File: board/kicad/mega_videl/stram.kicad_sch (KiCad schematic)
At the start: 3 parts

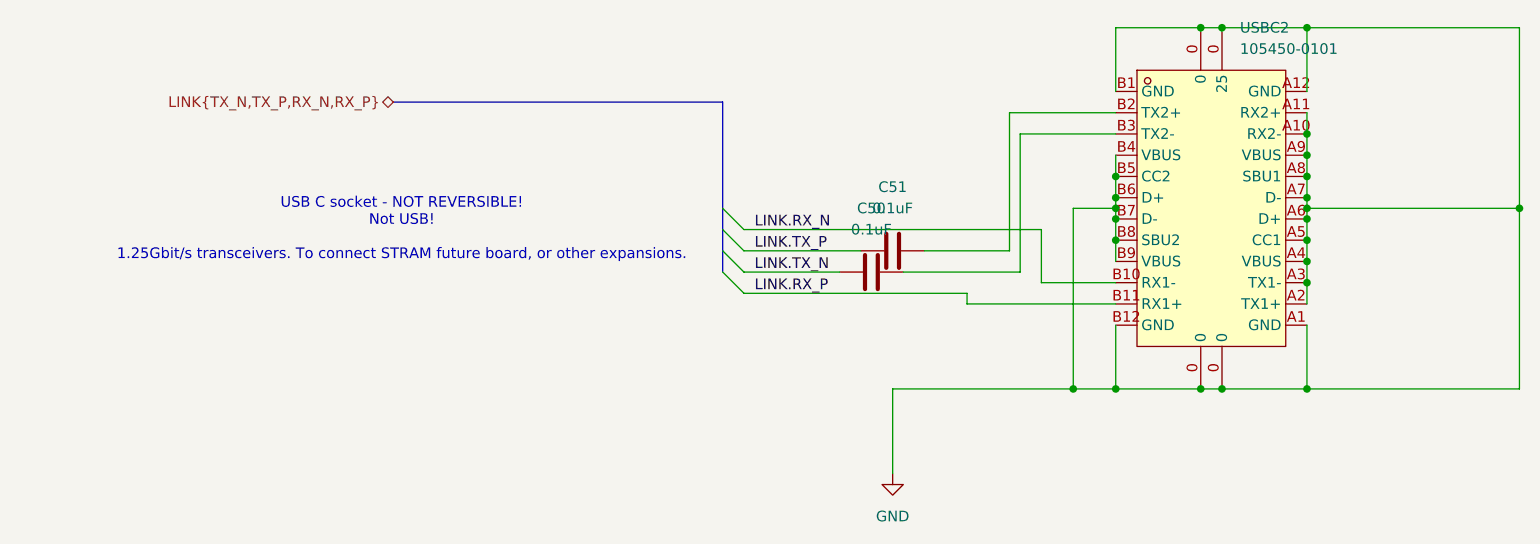
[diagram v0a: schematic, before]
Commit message: Reviewed and fixed many issues. e.g. missing decoupling for 1.35v under fpga
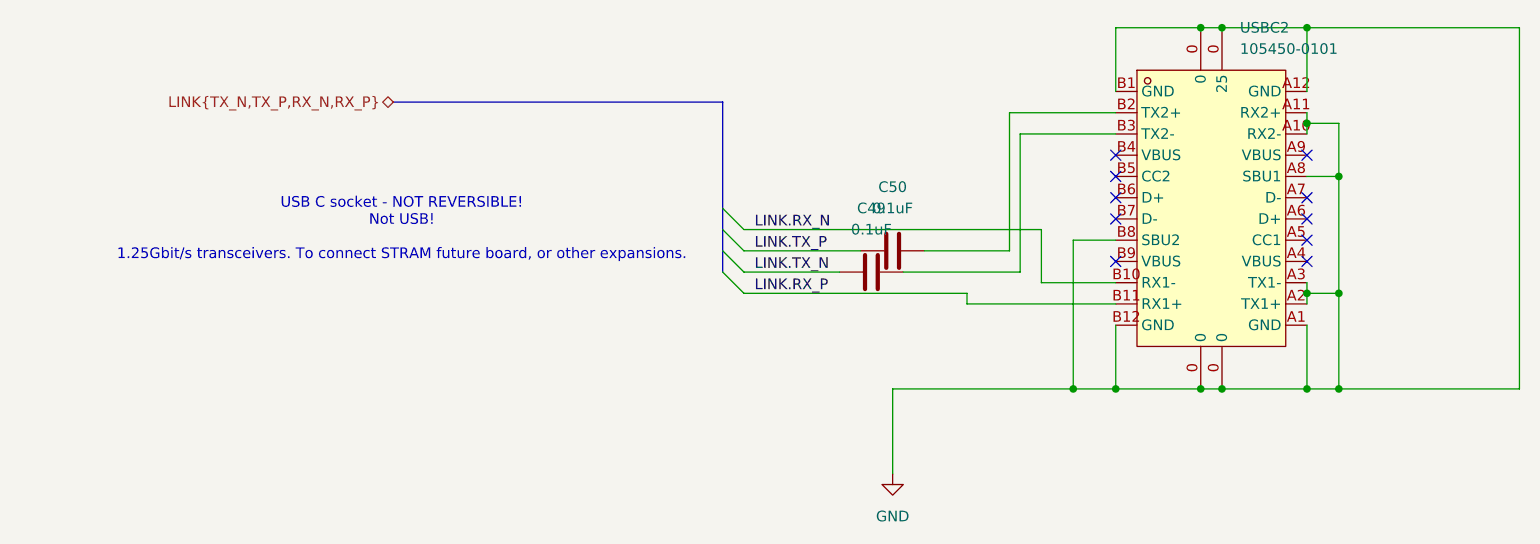
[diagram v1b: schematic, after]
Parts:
- renumbered C50 to C49, C51 to C50
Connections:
- net GND: no longer USBC2.A4 (VBUS), USBC2.A5 (CC1), USBC2.A6 (D+), USBC2.A7 (D-), USBC2.A9 (VBUS), USBC2.B4 (VBUS), USBC2.B5 (CC2), USBC2.B6 (D+), USBC2.B7 (D-), USBC2.B9 (VBUS)
- no-connect marks 0 -> 10

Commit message: Assigned all parts with JLCPCB plugin
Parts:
- C49, C50: LCSC (none) -> C14663
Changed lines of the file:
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@@
+			)
+		)
+		(property "LCSC" "C14663"
+			(at 110.49 77.47 0)
+			(hide yes)
+			(show_name no)
+			(do_not_autoplace no)
+			(effects
+				(font
+					(size 1.27 1.27)
+				)
 			)
 		)
@@
 			(at 113.03 74.93 0)
 			(hide yes)
+			(show_name no)
+			(do_not_autoplace no)
+			(effects
+				(font
+					(size 1.27 1.27)
+				)
+			)
+		)
+		(property "LCSC" "C14663"
+			(at 113.03 74.93 0)
+			(hide yes)
